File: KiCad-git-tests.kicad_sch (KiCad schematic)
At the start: 2 parts

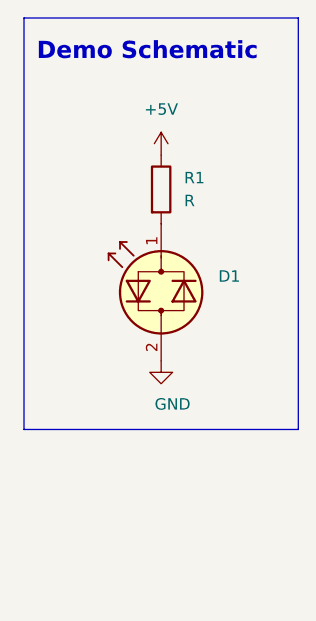
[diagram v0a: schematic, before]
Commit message: duplicate resistor
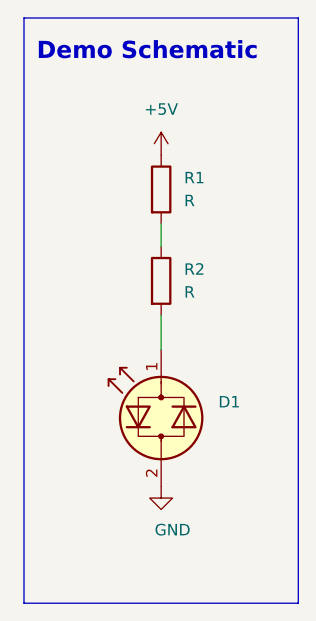
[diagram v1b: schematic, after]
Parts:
- added R2: R, Resistor_SMD:R_0612_1632Metric, symbol Device:R
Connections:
- net at R1.2: now also R2.1; no longer D1.1 (KA)
- new net: D1.1 (KA), R2.2
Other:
- moved on the sheet: D1
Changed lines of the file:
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@@
 	(rectangle
 		(start 78.74 20.32)
-		(end 109.22 66.04)
+		(end 109.22 85.344)
 		(stroke
 			(width 0)
@@
 		)
 	)
+	(wire
+		(pts
+			(xy 93.98 53.34) (xy 93.98 57.15)
+		)
+		(stroke
+			(width 0)
+			(type default)
+		)
+	)
+	(wire
+		(pts
+			(xy 93.98 43.18) (xy 93.98 45.72)
+		)
+		(stroke
+			(width 0)
+			(type default)
+		)
+	)
+	(symbol
+		(lib_id "Device:R")
+		(at 93.98 49.53 0)
+		(unit 1)
+		(body_style 1)
+		(exclude_from_sim no)
+		(in_bom yes)
+		(on_board yes)
+		(in_pos_files yes)
+		(dnp no)
+		(fields_autoplaced yes)
+		(property "Reference" "R2"
+			(at 96.52 48.2599 0)
+			(show_name no)
+			(do_not_autoplace no)
+			(effects
+				(font
+					(size 1.27 1.27)
+				)
+				(justify left)
+			)
+		)
+		(property "Value" "R"
+			(at 96.52 50.7999 0)
+			(show_name no)
+			(do_not_autoplace no)
+			(effects
+				(font
+					(size 1.27 1.27)
+				)
+				(justify left)
+			)
+		)
+		(property "Footprint" "Resistor_SMD:R_0612_1632Metric"
+			(at 92.202 49.53 90)
+			(hide yes)
+			(show_name no)
+			(do_not_autoplace no)
+			(effects
+				(font
+					(size 1.27 1.27)
+				)
+			)
+		)
+		(property "Datasheet" ""
+			(at 93.98 49.53 0)
+			(hide yes)
+			(show_name no)
+			(do_not_autoplace no)
+			(effects
+				(font
+					(size 1.27 1.27)
+				)
+			)
+		)
+		(property "Description" "Resistor"
+			(at 93.98 49.53 0)
+			(hide yes)
+			(show_name no)
+			(do_not_autoplace no)
+			(effects
+				(font
+					(size 1.27 1.27)
+				)
+			)
+		)
+		(pin "1"
+		)
+		(pin "2"
+		)
+		(instances
+			(project "KiCad-git-tests"
+				(path "/e63e39d7-6ac0-4ffd-8aa3-1841a4541b55"
+					(reference "R2")
+					(unit 1)
+				)
+			)
+		)
+	)
 	(symbol
 		(lib_id "Device:LED_Dual_Bidirectional")
-		(at 93.98 50.8 90)
+		(at 93.98 64.77 90)
 		(unit 1)
 		(body_style 1)
@@
 		(fields_autoplaced yes)
 		(property "Reference" "D1"
-			(at 100.33 49.0346 90)
+			(at 100.33 63.0046 90)
 			(show_name no)
 			(do_not_autoplace no)
@@
 		)
 		(property "Value" "LED_Dual_Bidirectional"
-			(at 100.33 51.5746 90)
+			(at 100.33 65.5446 90)
 			(hide yes)
 			(show_name no)
@@
 		)
 		(property "Footprint" "LED_SMD:LED_1812_4532Metric_Pad1.30x3.40mm_HandSolder"
-			(at 93.98 50.8 0)
+			(at 93.98 64.77 0)
 			(hide yes)
 			(show_name no)
@@
 		)
 		(property "Datasheet" ""
-			(at 93.98 50.8 0)
+			(at 93.98 64.77 0)
 			(hide yes)
 			(show_name no)
@@
 		)
 		(property "Description" "Dual LED, bidirectional"
-			(at 93.98 50.8 0)
+			(at 93.98 64.77 0)
 			(hide yes)
 			(show_name no)
@@
 	(symbol
 		(lib_id "power:GND")
-		(at 93.98 58.42 0)
+		(at 93.98 72.39 0)
 		(unit 1)
 		(body_style 1)
@@
 		(dnp no)
 		(property "Reference" "#PWR02"
-			(at 93.98 64.77 0)
+			(at 93.98 78.74 0)
 			(hide yes)
 			(show_name no)
@@
 		)
 		(property "Value" "GND"
-			(at 95.25 63.246 0)
+			(at 95.25 77.216 0)
 			(show_name no)
 			(do_not_autoplace no)
@@
 		)
 		(property "Footprint" ""
-			(at 93.98 58.42 0)
+			(at 93.98 72.39 0)
 			(hide yes)
 			(show_name no)
@@
 		)
 		(property "Datasheet" ""
-			(at 93.98 58.42 0)
+			(at 93.98 72.39 0)
 			(hide yes)
 			(show_name no)
@@
 		)
 		(property "Description" "Power symbol creates a global label with name \"GND\" , ground"
-			(at 93.98 58.42 0)
-			(hide yes)
-			(show_name no)
+			(at 93.98 72.39 0)
+			(hide yes)
+			(show_name no)
